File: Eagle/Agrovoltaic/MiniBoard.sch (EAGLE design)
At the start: 188 parts, among them J1 WAGO-03BE, J2 WAGO-03BE, J3 WAGO-03BE, K1 SRD-05VDC-SL-C, K3 SRD-05VDC-SL-C, Q1 BC338, Q2 BC338, U1 ESP32-DEVKIT-V1

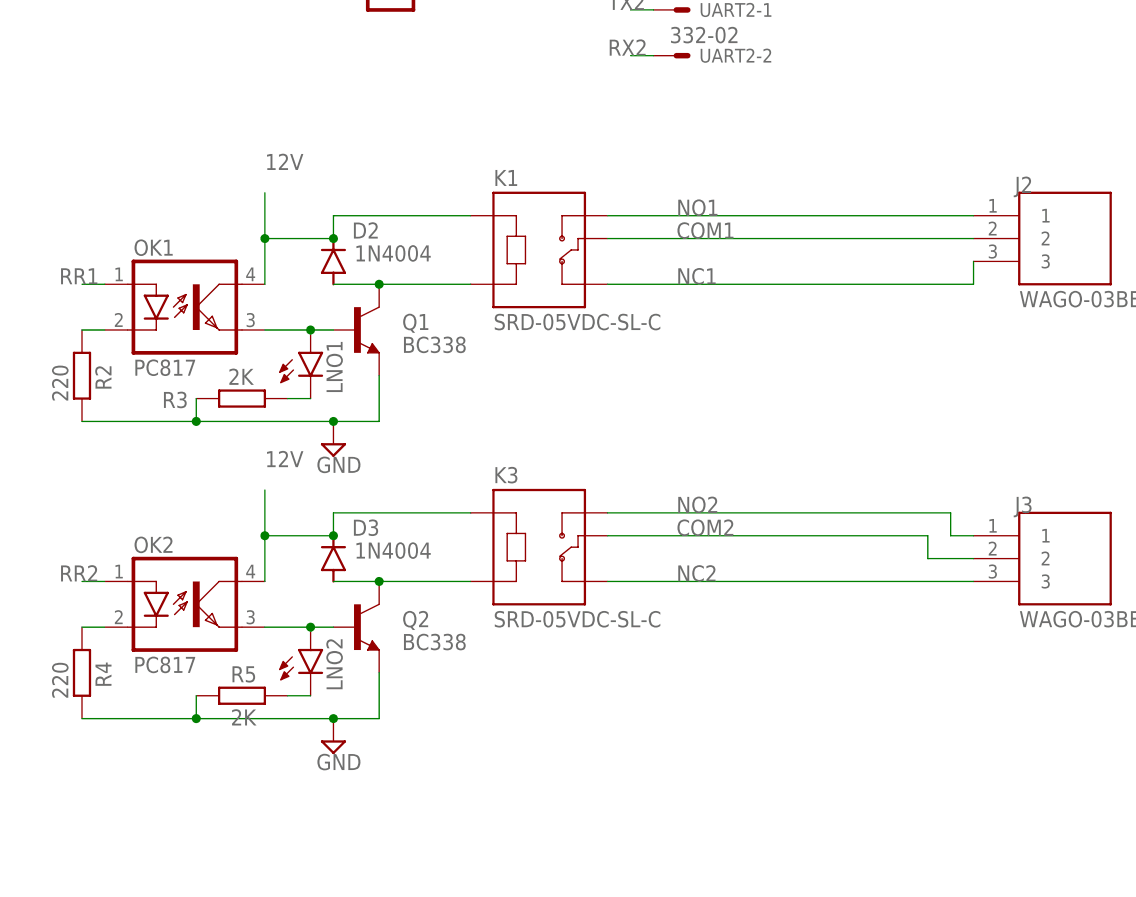
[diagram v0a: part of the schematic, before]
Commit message: Revisi lagi lamp ke colector relay
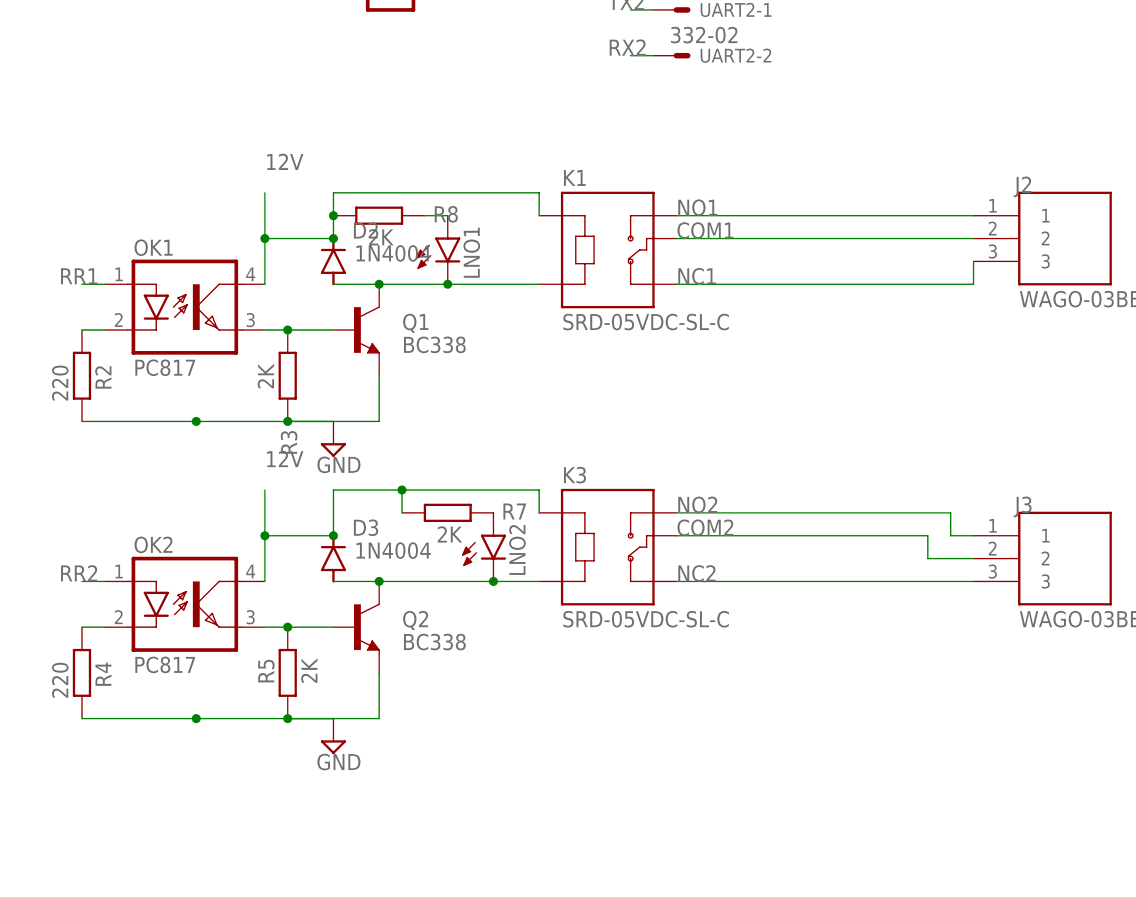
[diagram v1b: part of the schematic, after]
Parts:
- added R7, R8: 2K, rcl-ws:R-EU_0309/12
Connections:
- removed net N$12: LNO1.C, R3.1
- new net N$11: D2.A, K1.A2, LNO1.C, Q1.C
- net 12V: now also R7.1, R8.1
- net N$10: now also LNO1.A, R8.2; no longer LNO2.C, R5.2
- net N$3: now also R3.1; no longer LNO1.A
- net N$4: now also D3.A, K3.A2, LNO2.C, Q2.C; no longer D2.A, K1.A2, Q1.C
- net N$6: now also R5.2; no longer LNO2.A
- net N$7: now also LNO2.A, R7.2; no longer D3.A, K3.A2, Q2.C
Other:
- moved on the sheet: K1, K3, LNO1, LNO2, R3, R5
